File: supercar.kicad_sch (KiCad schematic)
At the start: 59 parts, among them SW1 Power, U1 74HC283, U2 74HC574, U3 74HC154, U4 74HC574, U5 74HC21, U6 74HC02, U7 74HC04, U8 NE555D

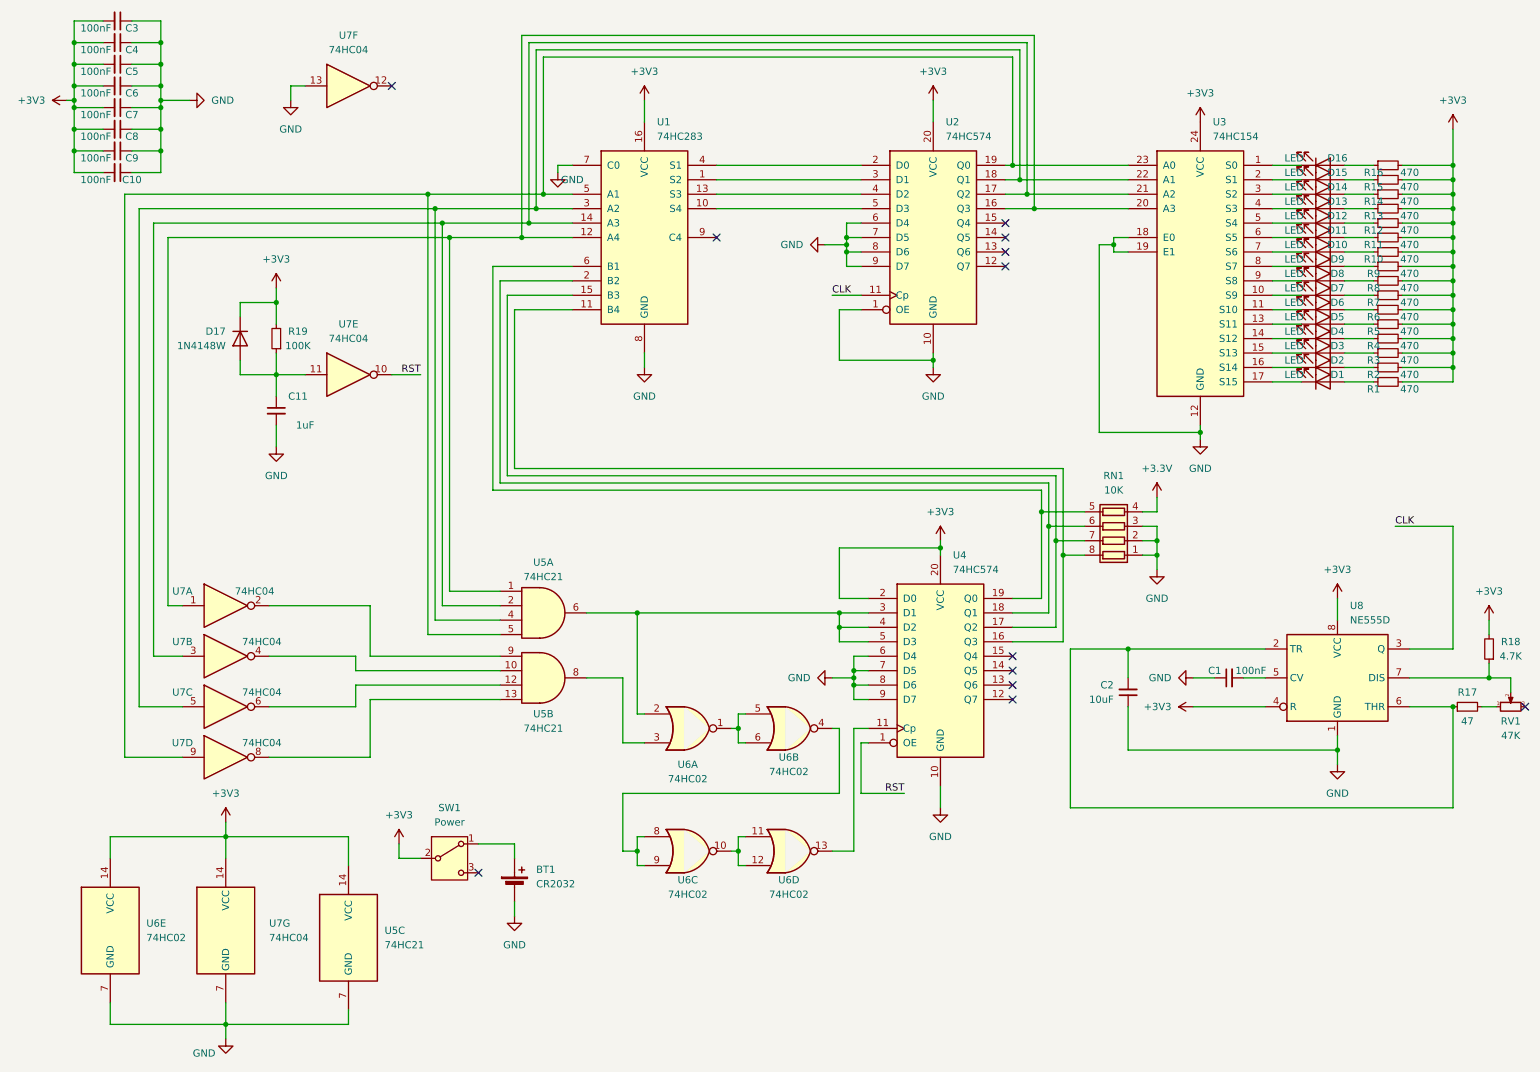
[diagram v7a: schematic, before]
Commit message: Reduce IC count and reroute the board
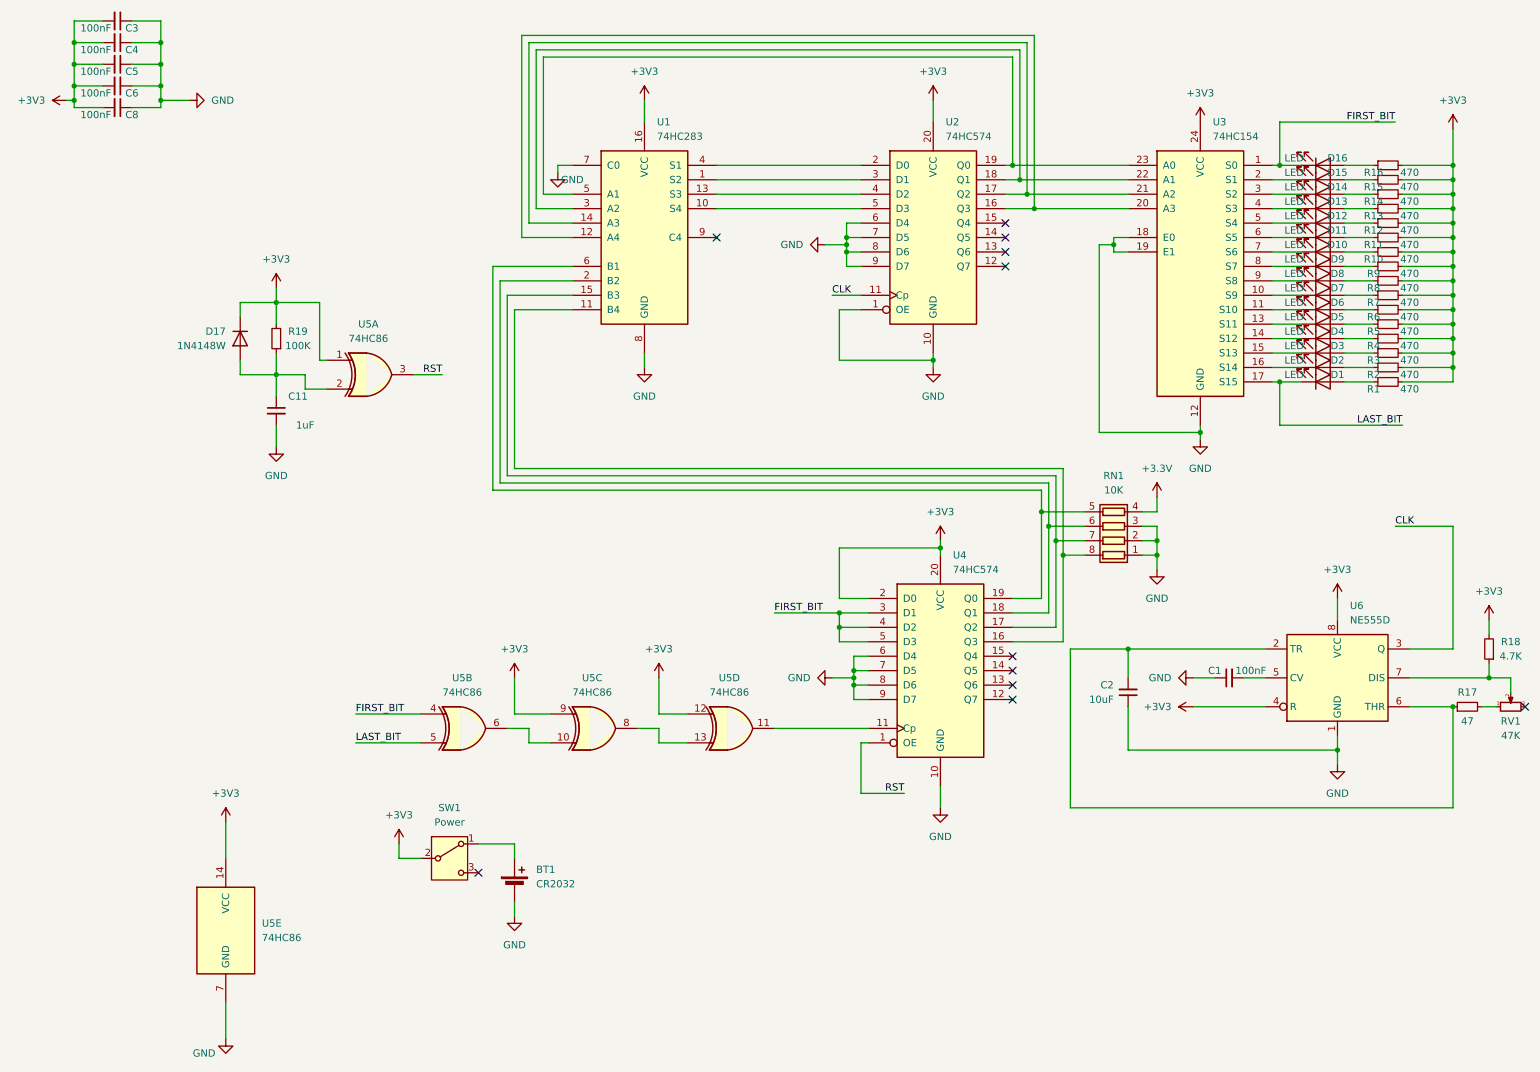
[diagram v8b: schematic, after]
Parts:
- removed C10, C7, C9: 100nF, Capacitor_SMD:C_1206_3216Metric_Pad1.33x1.80mm_HandSolder, symbol Device:C_Small
- removed U5: 74HC21, Package_SO:SOIC-14_3.9x8.7mm_P1.27mm, symbol 74xx:74LS21
- removed U6: 74HC02, Package_SO:SOIC-14_3.9x8.7mm_P1.27mm, symbol 74xx:74HC02
- removed U7: 74HC04, Package_SO:SOIC-14_3.9x8.7mm_P1.27mm, symbol 74xx:74HC04
- added U5: 74HC86, Package_SO:SOIC-14_3.9x8.7mm_P1.27mm, symbol 74xx:74HC86
- renumbered U8 to U6
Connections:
- net +3V3: now also U5.1, U5.12, U5.14 (VCC), U5.9
- net GND: now also U5.7 (GND)
- net RST: now also U5.3
- net FIRST_BIT: now reaches U4.3 (D1), U4.4 (D2), U4.5 (D3)
- net FIRST_BIT: now also D16.1 (K), U3.1 (S0), U5.4
- net at U4.11 (Cp): now also U5.11
- net LAST_BIT: now reaches D1.1 (K), U3.17 (S15)
- net LAST_BIT: now also U5.5
- net at C11.1, D17.2 (A), R19.1: now also U5.2
- new net: U5.10, U5.6
- new net: U5.13, U5.8
- no-connect marks 12 -> 11
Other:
- moved on the sheet: C8
